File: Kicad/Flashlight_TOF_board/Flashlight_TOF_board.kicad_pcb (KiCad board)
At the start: 2 copper layers, 33 x 16 mm, 28 parts, among them IC1 PI4ULS3V204ZBEX, IC2 LDK130M18RY, IC3 PI4ULS3V204ZBEX, J1 F52R-1A7H1-11008, U1 VL53L8CXV0GC_1

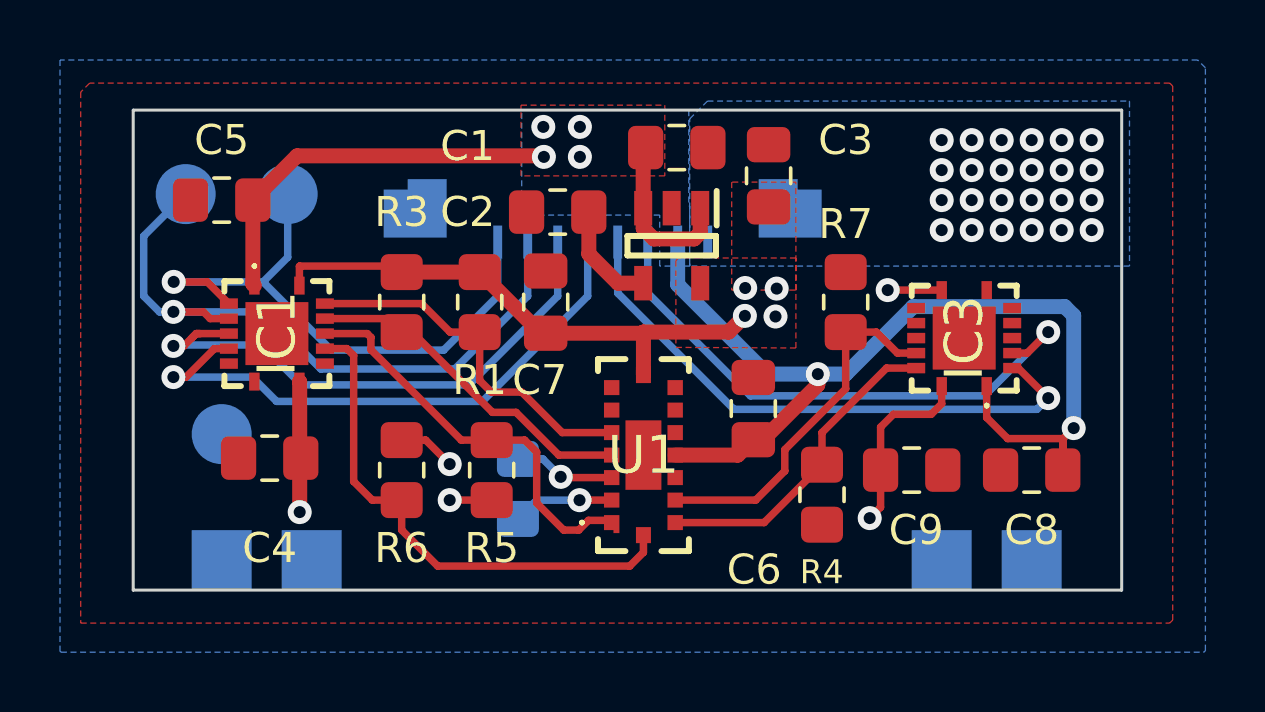
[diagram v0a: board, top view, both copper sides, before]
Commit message: cosmetic work on tof
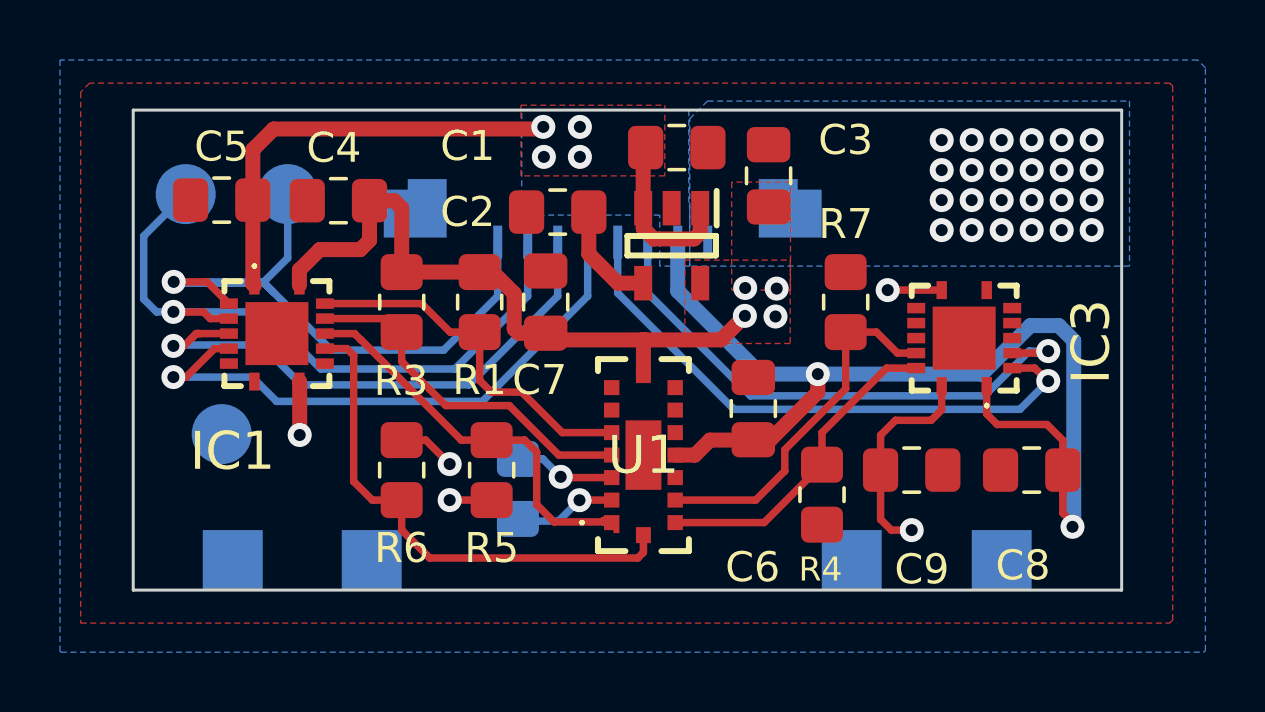
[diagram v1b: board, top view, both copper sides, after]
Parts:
- moved C4 8.88 mm to (128.9, 62.0)
- moved WELD 3.00 mm to (146.0, 74.0)
- moved WELD 2.00 mm to (130.0, 74.0)
- moved WELD 1.00 mm to (151.0, 74.0)
- moved WELD 0.37 mm to (125.4, 74.0)
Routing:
- net +3V3: track 53.8 -> 58.9 mm
- net SCLCK: track 19.7 -> 23.2 mm
- net +1V8: track 37.3 -> 40.1 mm
- net NCS: track 18.8 -> 18.3 mm
